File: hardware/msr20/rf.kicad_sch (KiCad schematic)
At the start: 9 parts, among them U6 74LS163, U7 CD74HC4046

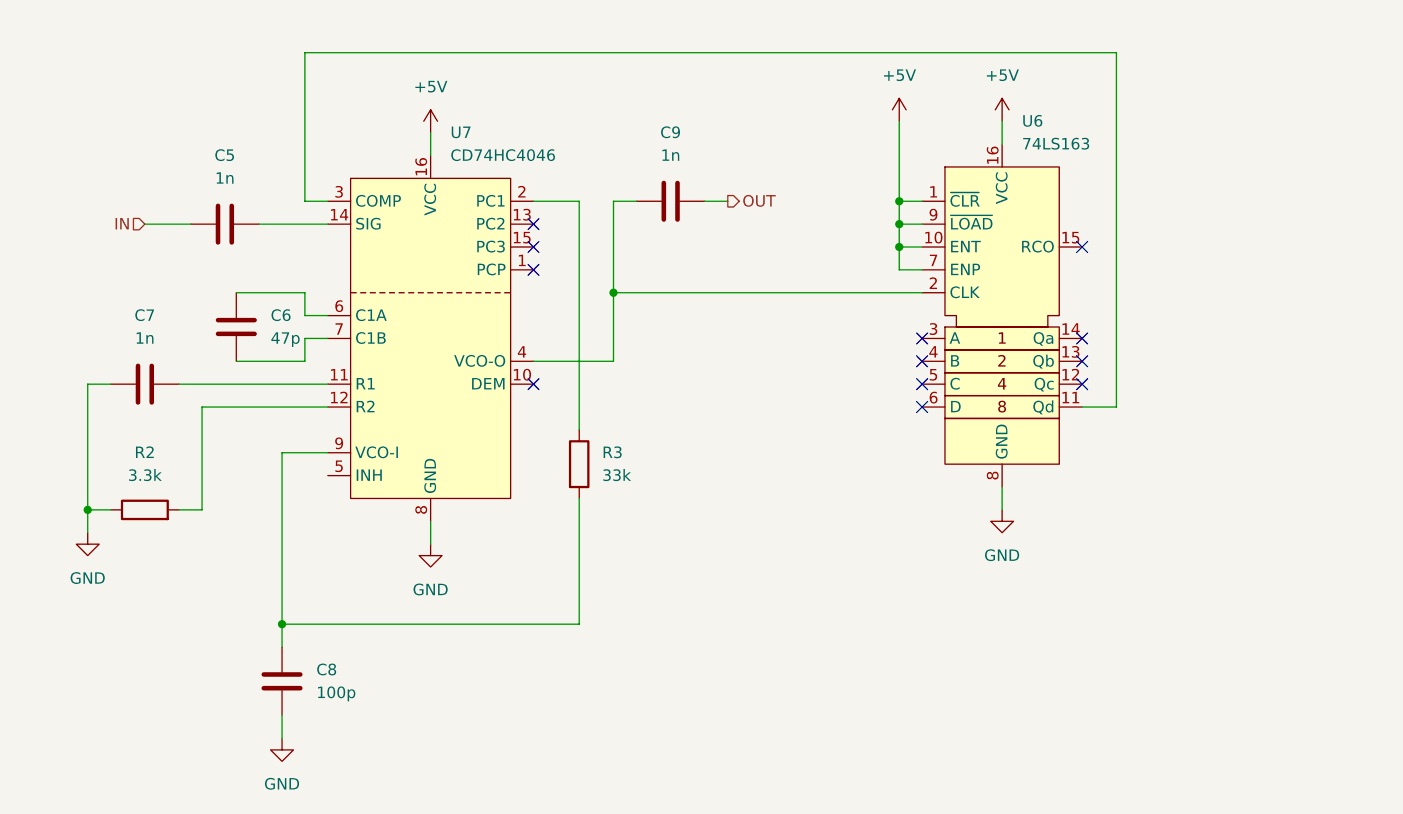
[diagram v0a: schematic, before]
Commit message: add if filter and if amplifier to schematic, organize into sheet hierarchy
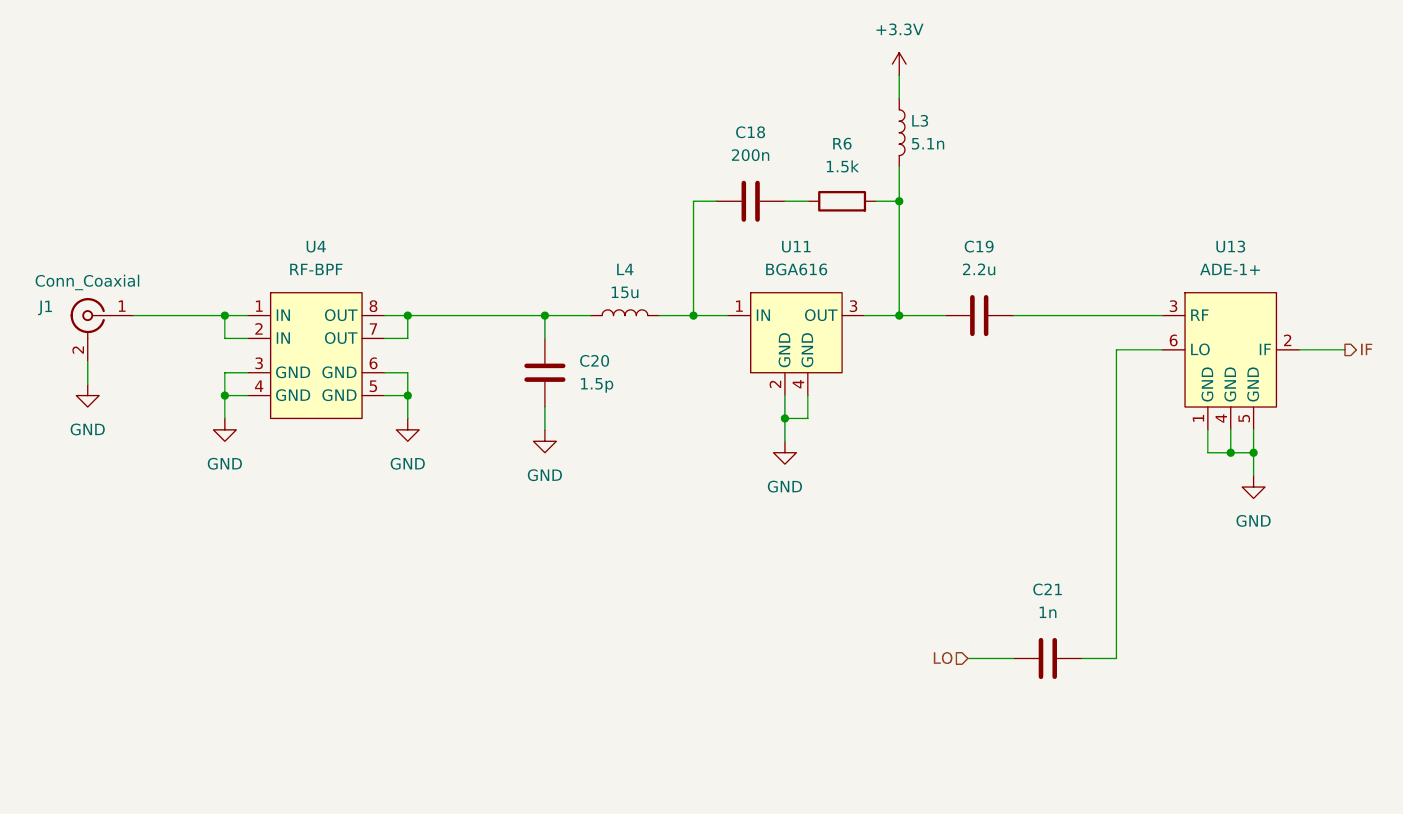
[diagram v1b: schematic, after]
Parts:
- removed C5, C7, C9: 1n, Capacitor_SMD:C_0805_2012Metric, symbol Device:C
- removed C6: 47p, Capacitor_SMD:C_0805_2012Metric, symbol Device:C
- removed C8: 100p, Capacitor_SMD:C_0805_2012Metric, symbol Device:C
- removed R2: 3.3k, Resistor_SMD:R_0805_2012Metric, symbol Device:R
- removed R3: 33k, Resistor_SMD:R_0805_2012Metric, symbol Device:R
- removed U6: 74LS163, Package_DIP:DIP-16_W7.62mm_LongPads, symbol msr20:74LS163
- removed U7: CD74HC4046, Package_DIP:DIP-16_W7.62mm_LongPads, symbol msr20:CD74HC4046
- added C18: 200n, Capacitor_SMD:C_0805_2012Metric, symbol Device:C
- added C19: 2.2u, Capacitor_SMD:C_0805_2012Metric, symbol Device:C
- added C20: 1.5p, Capacitor_SMD:C_0805_2012Metric, symbol Device:C
- added C21: 1n, Capacitor_SMD:C_0805_2012Metric, symbol Device:C
- added J1: Conn_Coaxial, Connector_Coaxial:BNC_Amphenol_B6252HB-NPP3G-50_Horizontal, symbol Connector:Conn_Coaxial
- added L3: 5.1n, Inductor_SMD:L_0805_2012Metric, symbol Device:L
- added L4: 15u, Inductor_SMD:L_0805_2012Metric, symbol Device:L
- added R6: 1.5k, Resistor_SMD:R_0805_2012Metric, symbol Device:R
- added U11: BGA616, msr20:BGA616, symbol msr20:BGA616
- added U13: ADE-1+, RF_Mini-Circuits:Mini-Circuits_CD636_H4.11mm, symbol msr20:ADE-1+
- added U4: RF-BPF, msr20:RF-BPF, symbol msr20:RF-BPF
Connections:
- net GND: now also C20.2, J1.2 (Ext), U11.2 (GND), U11.4 (GND), U13.1 (GND), U13.4 (GND), U13.5 (GND), U4.3 (GND), U4.4 (GND), U4.5 (GND), U4.6 (GND)
- new net: C19.1, L3.2, R6.2, U11.3 (OUT)
- new net: C18.2, R6.1
- new net: C18.1, L4.2, U11.1 (IN)
- new net: C20.1, L4.1, U4.7 (OUT), U4.8 (OUT)
- new net: C21.2, U13.6 (LO)
- new net: C19.2, U13.3 (RF)
- new net: J1.1 (In), U4.1 (IN), U4.2 (IN)
- new net +3.3V: L3.1
- new net IF: U13.2 (IF)
- new net LO: C21.1
- no-connect marks 12 -> 0
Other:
- title: Phase-Locked Loop -> (none)

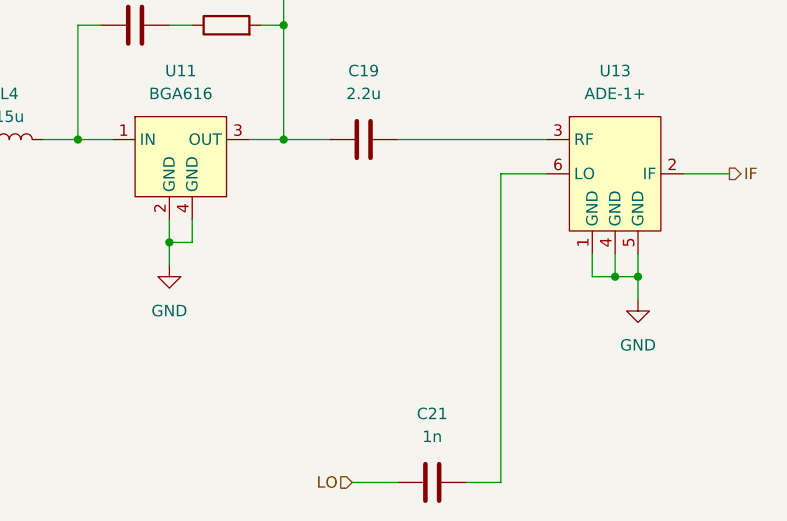
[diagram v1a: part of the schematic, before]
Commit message: add if section to pcb
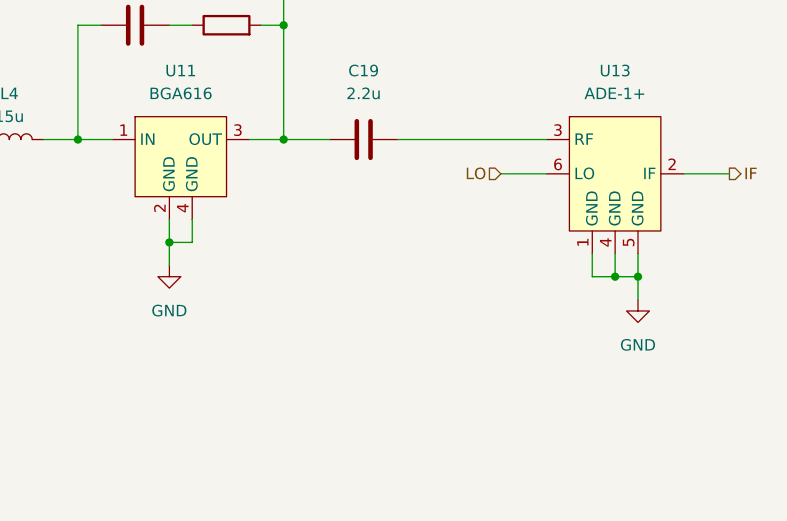
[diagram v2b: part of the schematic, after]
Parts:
- removed C21: 1n, Capacitor_SMD:C_0805_2012Metric, symbol Device:C
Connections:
- net LO: now also U13.6 (LO)
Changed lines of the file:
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@@
-	(wire
-		(pts
-			(xy 161.29 127) (xy 166.37 127)
-		)
-		(stroke
-			(width 0)
-			(type default)
-		)
-	)
 	(wire
 		(pts
@@
 	(wire
 		(pts
-			(xy 177.8 127) (xy 173.99 127)
-		)
-		(stroke
-			(width 0)
-			(type default)
-		)
-	)
-	(wire
-		(pts
 			(xy 99.06 88.9) (xy 96.52 88.9)
 		)
@@
 		(pts
 			(xy 143.51 100.33) (xy 140.97 100.33)
-		)
-		(stroke
-			(width 0)
-			(type default)
-		)
-	)
-	(wire
-		(pts
-			(xy 177.8 92.71) (xy 177.8 127)
 		)
 		(stroke
@@
 	(hierarchical_label "LO"
 		(shape input)
-		(at 161.29 127 180)
+		(at 177.8 92.71 180)
 		(fields_autoplaced yes)
 		(effects
@@
 					(unit 1)
 				)
-			)
-		)
-	)
-	(symbol
-		(lib_id "Device:C")
-		(at 170.18 127 90)
-		(unit 1)
-		(exclude_from_sim no)
-		(in_bom yes)
-		(on_board yes)
-		(dnp no)
-		(fields_autoplaced yes)
-		(property "Reference" "C21"
-			(at 170.18 119.38 90)
-			(effects
-				(font
-					(size 1.27 1.27)
-				)
-			)
-		)
-		(property "Value" "1n"
-			(at 170.18 121.92 90)
-			(effects
-				(font
-					(size 1.27 1.27)
-				)
-			)
-		)
-		(property "Footprint" "Capacitor_SMD:C_0805_2012Metric"
-			(at 173.99 126.0348 0)
-			(effects
-				(font
-					(size 1.27 1.27)
-				)
-				(hide yes)
-			)
-		)
-		(property "Datasheet" "~"
-			(at 170.18 127 0)
-			(effects
-				(font
-					(size 1.27 1.27)
-				)
-				(hide yes)
-			)
-		)
-		(property "Description" "Unpolarized capacitor"
-			(at 170.18 127 0)
-			(effects
-				(font
-					(size 1.27 1.27)
-				)
-				(hide yes)
-			)
-		)
-		(pin "2"
-		)
-		(pin "1"
-		)
-		(instances
-			(project "msr20"
-				(path "/827e4c90-6b76-4aba-b6da-8b66ea005818/d4efeb94-5cf1-43a2-925a-fd36115a5e3e"
-					(reference "C21")
-					(unit 1)
-				)

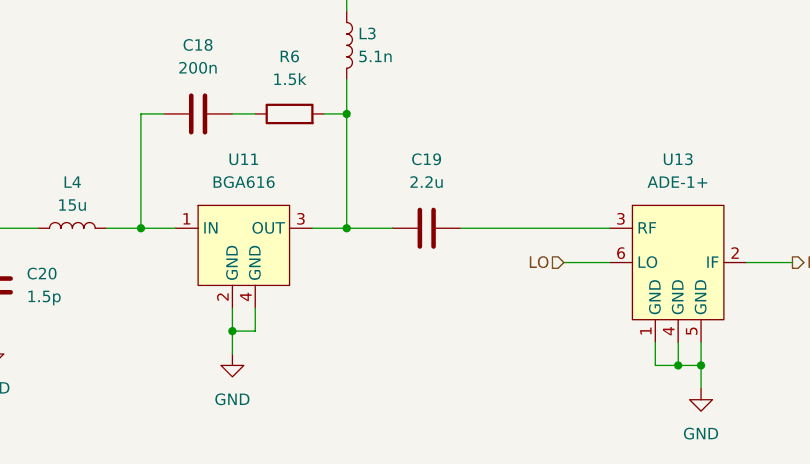
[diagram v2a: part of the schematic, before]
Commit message: add test points to schematic
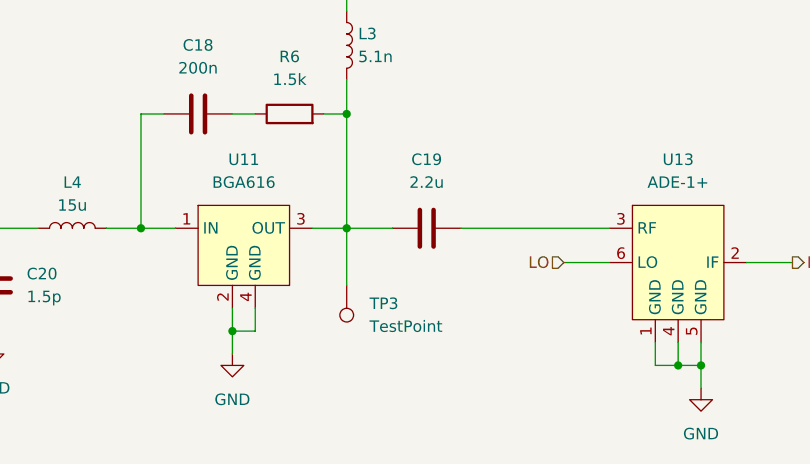
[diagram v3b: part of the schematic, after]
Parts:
- added TP3: TestPoint, TestPoint:TestPoint_Pad_D1.0mm, symbol Connector:TestPoint
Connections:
- net at C19.1, L3.2, R6.2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: now also TP3.1
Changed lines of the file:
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@@
+	(wire
+		(pts
+			(xy 153.67 88.9) (xy 153.67 95.25)
+		)
+		(stroke
+			(width 0)
+			(type default)
+		)
+	)
 	(wire
 		(pts
@@
 					(unit 1)
 				)
+			)
+		)
+	)
+	(symbol
+		(lib_id "Connector:TestPoint")
+		(at 153.67 95.25 180)
+		(unit 1)
+		(exclude_from_sim no)
+		(in_bom yes)
+		(on_board yes)
+		(dnp no)
+		(fields_autoplaced yes)
+		(property "Reference" "TP3"
+			(at 156.21 97.2819 0)
+			(effects
+				(font
+					(size 1.27 1.27)
+				)
+				(justify right)
+			)
+		)
+		(property "Value" "TestPoint"
+			(at 156.21 99.8219 0)
+			(effects
+				(font
+					(size 1.27 1.27)
+				)
+				(justify right)
+			)
+		)
+		(property "Footprint" "TestPoint:TestPoint_Pad_D1.0mm"
+			(at 148.59 95.25 0)
+			(effects
+				(font
+					(size 1.27 1.27)
+				)
+				(hide yes)
+			)
+		)
+		(property "Datasheet" "~"
+			(at 148.59 95.25 0)
+			(effects
+				(font
+					(size 1.27 1.27)
+				)
+				(hide yes)
+			)
+		)
+		(property "Description" "test point"
+			(at 153.67 95.25 0)
+			(effects
+				(font
+					(size 1.27 1.27)
+				)
+				(hide yes)
+			)
+		)
+		(pin "1"
+		)
+		(instances
+			(project "msr20"
+				(path "/827e4c90-6b76-4aba-b6da-8b66ea005818/d4efeb94-5cf1-43a2-925a-fd36115a5e3e"
+					(reference "TP3")
+					(unit 1)
+				)
